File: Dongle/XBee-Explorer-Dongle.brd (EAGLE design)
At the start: 40.6 x 27.9 mm, 30 parts, among them U2 XBEE-1B3, U3 V_REG_LDOSMD, U4 FT231XS

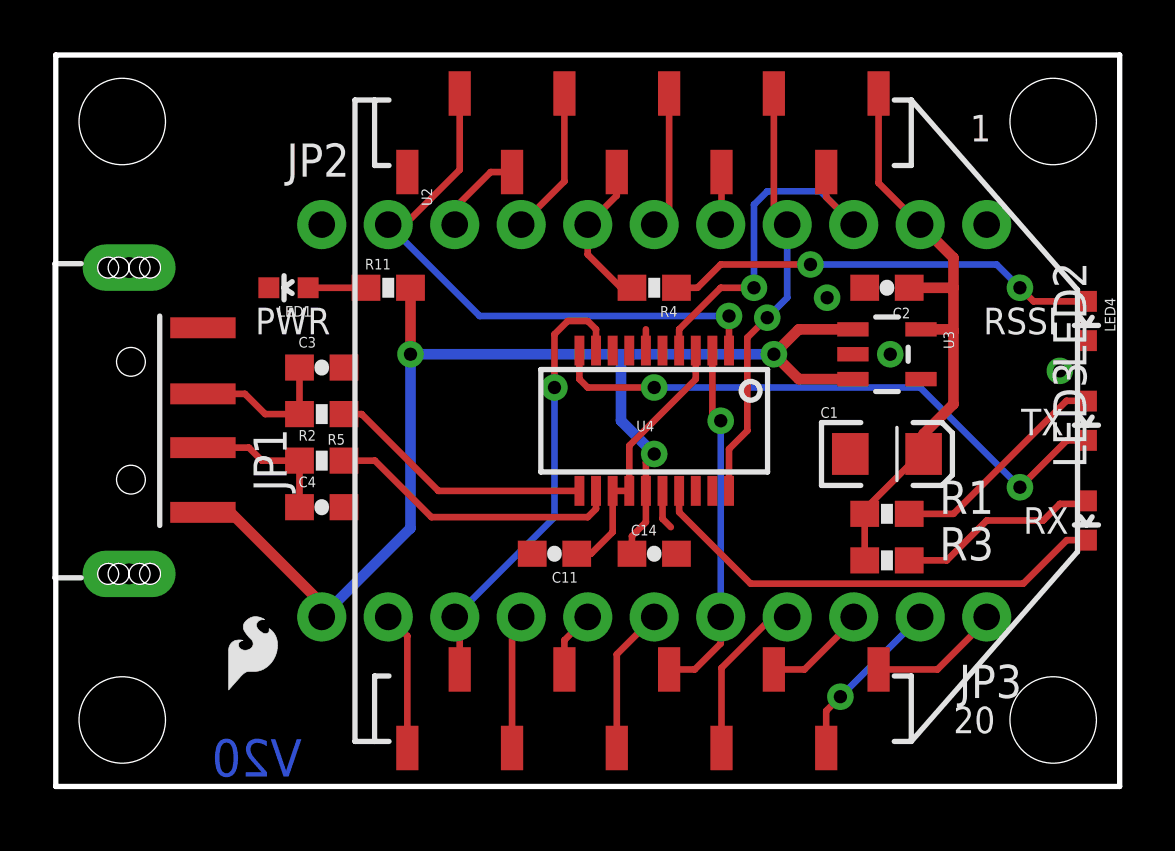
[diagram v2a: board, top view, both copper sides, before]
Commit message: Added jumper to disconnect RSSI LED, moved silk
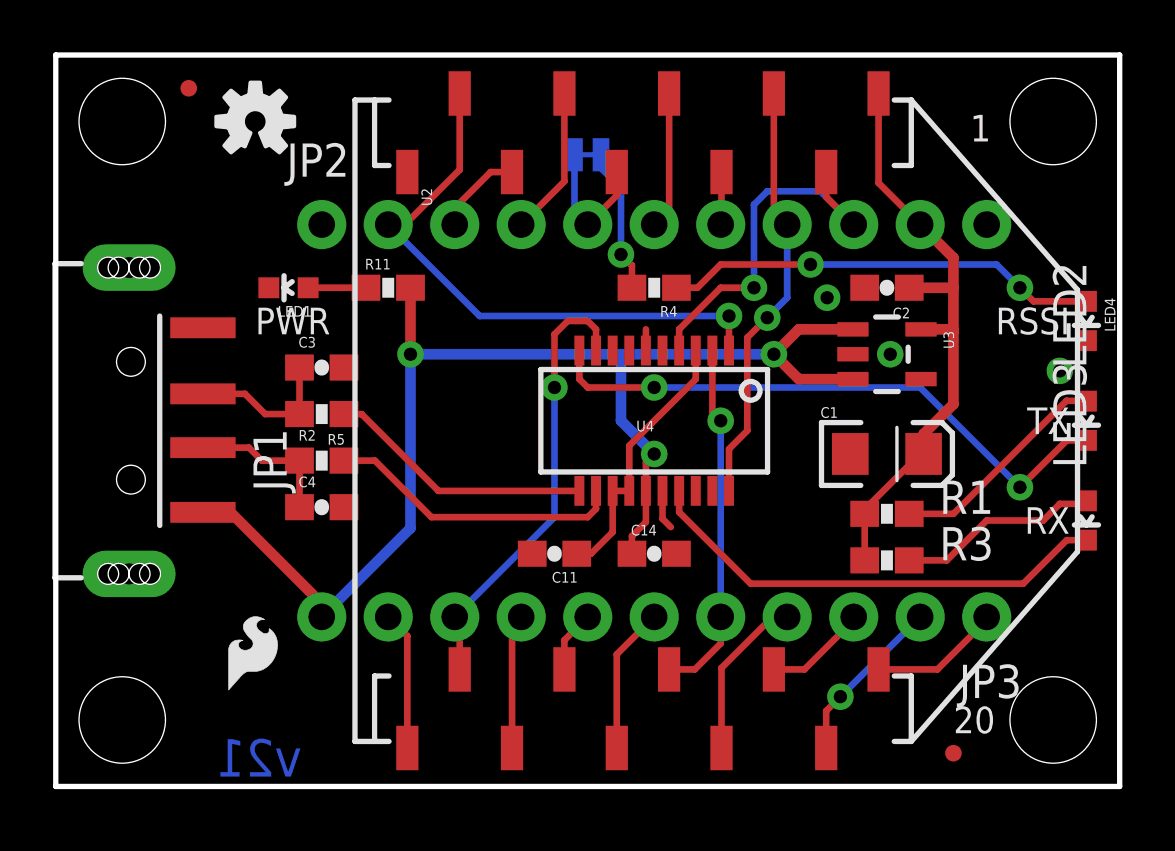
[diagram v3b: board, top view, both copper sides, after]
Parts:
- added FID1, FID2: FIDUCIALUFIDUCIAL, SparkFun-Aesthetics:MICRO-FIDUCIAL
- added FRAME1: FRAME-LETTER, SparkFun-Aesthetics:CREATIVE_COMMONS
- added SJ1: RSSI, SparkFun-Passives:SJ_2S-TRACE
- U$7: value CREATIVE_COMMONS -> OSHW-LOGOS; device SparkFun:CREATIVE_COMMONS -> SparkFun:OSHW-LOGO-S
- U3: value V_REG_LDOSMD -> MIC5205 3.3V
- moved U$7 34.3 mm to (7.62, 25.4)
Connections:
- new net N$8: R4.2, SJ1.2
- net RSSI: now also SJ1.1; no longer R4.2
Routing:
- net N$8: track 0.00 -> 5.57 mm, vias 0 -> 1
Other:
- board text added: "Nathan Seidle, Jim Lindblom"
- board text added: "RSSI LED"
- board text added: "v21"
- board text removed: "V20"
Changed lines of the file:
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@@
 <?xml version="1.0" encoding="utf-8"?>
 <!DOCTYPE eagle SYSTEM "eagle.dtd">
-<eagle version="6.4">
+<eagle version="6.5.0">
 <drawing>
 <settings>
@@
 <layer number="28" name="bValues" color="7" fill="1" visible="no" active="yes"/>
 <layer number="29" name="tStop" color="7" fill="3" visible="no" active="yes"/>
-<layer number="30" name="bStop" color="7" fill="6" visible="no" active="yes"/>
+<layer number="30" name="bStop" color="7" fill="6" visible="yes" active="yes"/>
 <layer number="31" name="tCream" color="7" fill="4" visible="no" active="yes"/>
 <layer number="32" name="bCream" color="7" fill="5" visible="no" active="yes"/>
@@
 <layer number="106" name="bPlate" color="7" fill="1" visible="no" active="yes"/>
 <layer number="107" name="Crop" color="7" fill="1" visible="no" active="yes"/>
+<layer number="108" name="tplace-old" color="10" fill="1" visible="yes" active="yes"/>
+<layer number="109" name="ref-old" color="11" fill="1" visible="yes" active="yes"/>
 <layer number="116" name="Patch_BOT" color="9" fill="4" visible="no" active="yes"/>
 <layer number="121" name="_tsilk" color="7" fill="1" visible="no" active="yes"/>
@@
 <wire x1="0" y1="0" x2="40.64" y2="0" width="0.2032" layer="20"/>
 <text x="7.62" y="17.272" size="1.016" layer="21" ratio="15">PWR</text>
-<text x="36.876" y="13.413" size="1.016" layer="21" ratio="15">TX</text>
-<text x="36.957" y="9.652" size="1.016" layer="21" ratio="15">RX</text>
-<text x="35.433" y="17.272" size="1.016" layer="21" ratio="15">RSSI</text>
+<text x="38.735" y="13.97" size="1.016" layer="21" ratio="15" align="center-right">TX</text>
+<text x="38.735" y="10.16" size="1.016" layer="21" ratio="15" align="center-right">RX</text>
+<text x="38.735" y="17.78" size="1.016" layer="21" ratio="15" align="center-right">RSSI</text>
 <text x="33.528" y="20.066" size="1.016" layer="22" ratio="15" rot="MR270">3.3V</text>
 <text x="30.988" y="20.066" size="1.016" layer="22" ratio="15" rot="MR270">DOUT</text>
@@
 <text x="9.652" y="7.874" size="1.016" layer="22" ratio="15" rot="MR90">5V</text>
 <text x="36.068" y="20.066" size="1.016" layer="22" ratio="15" rot="MR270">GND</text>
-<text x="9.398" y="0.381" size="1.4224" layer="16" font="vector" ratio="20" rot="MR0">V20</text>
+<text x="9.398" y="0.381" size="1.4224" layer="16" font="vector" ratio="20" rot="MR0">v21</text>
+<text x="20.32" y="25.908" size="0.889" layer="22" font="vector" ratio="15" rot="MR0" align="center">RSSI LED</text>
+<wire x1="19.812" y1="24.13" x2="20.828" y2="24.13" width="0.4064" layer="30"/>
+<text x="36.83" y="-8.89" size="1.778" layer="51">Nathan Seidle, Jim Lindblom</text>
 </plain>
 <attributes>
@@
 <attribute name="VALUE" x="20.574" y="18.923" size="0.4064" layer="27"/>
 </element>
-<element name="U3" library="SparkFun" package="SOT23-5" value="V_REG_LDOSMD" x="31.75" y="16.51" rot="R270"/>
+<element name="U3" library="SparkFun" package="SOT23-5" value="MIC5205 3.3V" x="31.75" y="16.51" rot="R270"/>
 <element name="C1" library="SparkFun" package="EIA3216" value="10uF" x="31.75" y="12.7"/>
 <element name="C2" library="SparkFun" package="0603-CAP" value="0.1uF" x="31.75" y="19.05" rot="R180"/>
 <element name="JP3" library="SparkFun" package="1X11_NO_SILK" value="M111X11_NO_SILK" x="35.56" y="6.477" rot="R180"/>
 <element name="JP2" library="SparkFun" package="1X11_NO_SILK" value="M111X11_NO_SILK" x="10.16" y="21.463"/>
-<element name="U$7" library="SparkFun" package="CREATIVE_COMMONS" value="CREATIVE_COMMONS" x="6.35" y="-8.89"/>
 <element name="U$8" library="SparkFun" package="OSHW-LOGO-S" value="OSHW-LOGOS" x="10.16" y="13.97" rot="MR0"/>
 <element name="JP1" library="SparkFun-Connectors" package="USB-A-SMT-MALE" value="USBA-SMD-MALE" x="2.54" y="13.97" rot="R90"/>
@@
 <element name="C3" library="SparkFun" package="0603-CAP" value="47pF" x="10.16" y="16.002"/>
 <element name="C4" library="SparkFun" package="0603-CAP" value="47pF" x="10.16" y="10.668"/>
+<element name="SJ1" library="SparkFun-Passives" package="SJ_2S-TRACE" value="RSSI" x="20.32" y="24.13" rot="MR180"/>
+<element name="FRAME1" library="SparkFun-Aesthetics" package="CREATIVE_COMMONS" value="FRAME-LETTER" x="6.35" y="-8.89"/>
+<element name="U$7" library="SparkFun" package="OSHW-LOGO-S" value="OSHW-LOGOS" x="7.62" y="25.4"/>
+<element name="FID1" library="SparkFun-Aesthetics" package="MICRO-FIDUCIAL" value="FIDUCIALUFIDUCIAL" x="5.08" y="26.67"/>
+<element name="FID2" library="SparkFun-Aesthetics" package="MICRO-FIDUCIAL" value="FIDUCIALUFIDUCIAL" x="34.29" y="1.27"/>
 </elements>
 <signals>
@@
 <signal name="RSSI">
 <contactref element="U2" pad="6"/>
-<contactref element="R4" pad="2"/>
 <contactref element="JP2" pad="5"/>
+<contactref element="SJ1" pad="1"/>
+<wire x1="19.812" y1="24.13" x2="19.812" y2="21.971" width="0.254" layer="16"/>
+<wire x1="19.812" y1="21.971" x2="20.32" y2="21.463" width="0.254" layer="16"/>
 <wire x1="21.43" y1="23.47" x2="21.43" y2="22.573" width="0.254" layer="1"/>
 <wire x1="21.43" y1="22.573" x2="20.32" y2="21.463" width="0.254" layer="1"/>
-<wire x1="22.01" y1="19.05" x2="21.59" y2="19.05" width="0.254" layer="1"/>
-<wire x1="21.59" y1="19.05" x2="20.32" y2="20.32" width="0.254" layer="1"/>
-<wire x1="20.32" y1="21.463" x2="20.32" y2="20.32" width="0.254" layer="1"/>
 </signal>
 <signal name="DIO12">
@@
 <wire x1="20.0025" y1="11.2903" x2="14.6177" y2="11.2903" width="0.254" layer="1"/>
 </signal>
+<signal name="N$8">
+<contactref element="R4" pad="2"/>
+<contactref element="SJ1" pad="2"/>
+<wire x1="20.828" y1="24.13" x2="20.828" y2="23.622" width="0.254" layer="16"/>
+<wire x1="20.828" y1="23.622" x2="21.59" y2="22.86" width="0.254" layer="16"/>
+<wire x1="21.59" y1="22.86" x2="21.59" y2="20.32" width="0.254" layer="16"/>
+<via x="21.59" y="20.32" extent="1-16" drill="0.508"/>
+<wire x1="21.59" y1="20.32" x2="22.01" y2="19.9" width="0.254" layer="1"/>
+<wire x1="22.01" y1="19.05" x2="22.01" y2="19.9" width="0.254" layer="1"/>
+</signal>
 </signals>

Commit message: Adding reset button, jumpers on UART ctrl lines
Reset button required moving LEDs around.
Adding jumpers on DTR, CTS, and RTS because they're not present on some
XBee compatible boards. Those pins can be used as GPIOs.
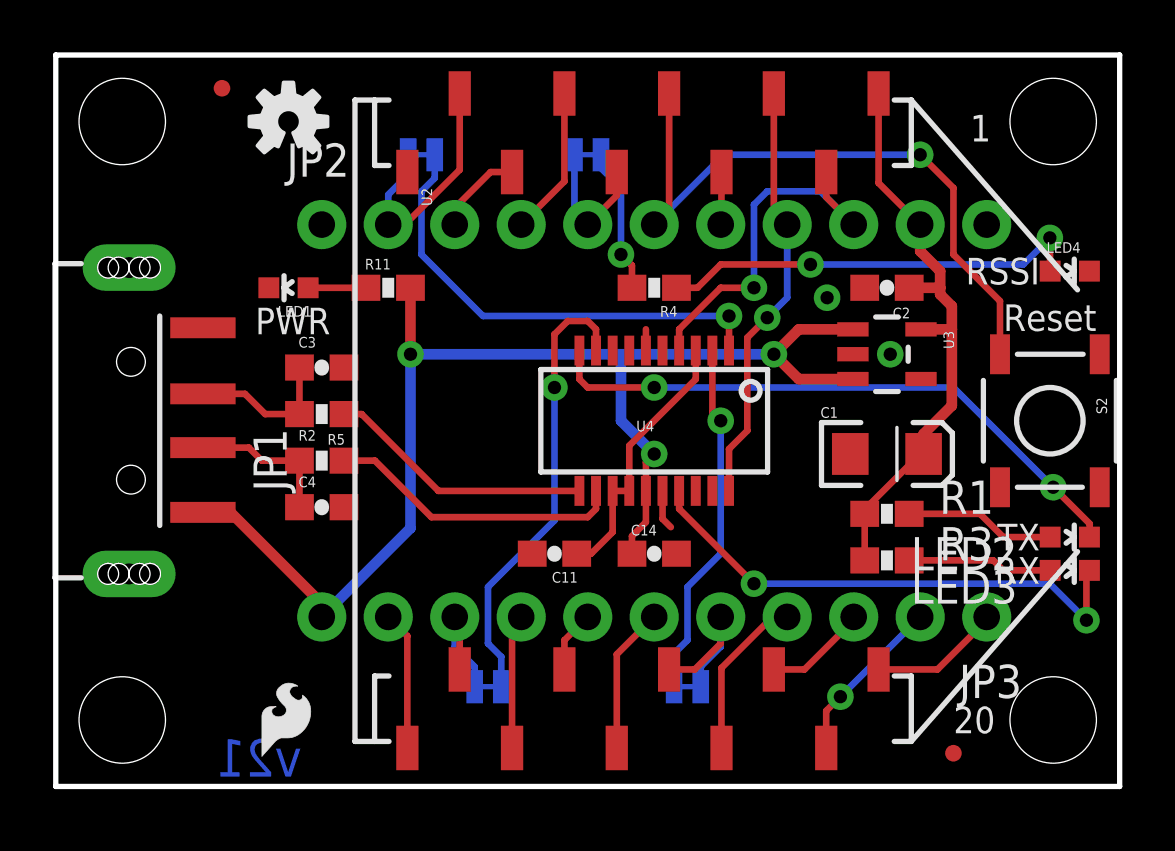
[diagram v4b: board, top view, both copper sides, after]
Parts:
- added S2: Reset, SparkFun-Electromechanical:TACTILE_SWITCH_SMD
- added SJ2, SJ3, SJ4: RSSI, SparkFun-Passives:SJ_2S-TRACE
- U2: device SparkFun:XBEE-SMD -> SparkFun-RF:XBEE-SMD
- moved LED2 4.49 mm to (38.7, 9.53), turned to 270 degrees
- moved U$1 2.84 mm to (7.87, 1.14)
- moved LED3 2.01 mm to (38.7, 8.26), turned to 270 degrees
- moved LED4 2.01 mm to (38.7, 19.7), turned to 270 degrees
- moved U$7 1.27 mm to (8.89, 25.4)
- moved FID1 1.27 mm to (6.35, 26.7)
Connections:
- new net CTS_XBEE: JP3.9, SJ3.2, U2.12
- new net DTR_XBEE: JP2.2, SJ4.2, U2.9
- new net RTS_XBEE: JP3.5, SJ2.2, U2.16
- net CTS: now also SJ3.1; no longer JP3.9, U2.12
- net DTR: now also SJ4.1; no longer JP2.2, U2.9
- net GND: now also S2.1
- net RESET: now also S2.3
- net RTS: now also SJ2.1; no longer JP3.5, U2.16
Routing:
- net RESET: track 5.24 -> 25.4 mm, vias 0 -> 1
- net DTR_XBEE: track 0.00 -> 9.49 mm
- net RTS_XBEE: track 0.00 -> 6.38 mm
- net CTS_XBEE: track 0.00 -> 5.07 mm
- net DTR: track 22.3 -> 18.1 mm
- net N$1: track 8.57 -> 5.75 mm
- net N$4: track 7.78 -> 5.54 mm
- net RXLED: track 18.2 -> 20.0 mm, vias 0 -> 2
- net 3.3V: track 23.5 -> 22.8 mm
- net GND: vias 3 -> 2
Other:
- board text added: "Reset"
- board text removed: "RSSI LED"
